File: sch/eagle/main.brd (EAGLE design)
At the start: 49.2 x 41.9 mm, 19 parts, among them IC1 LM339N

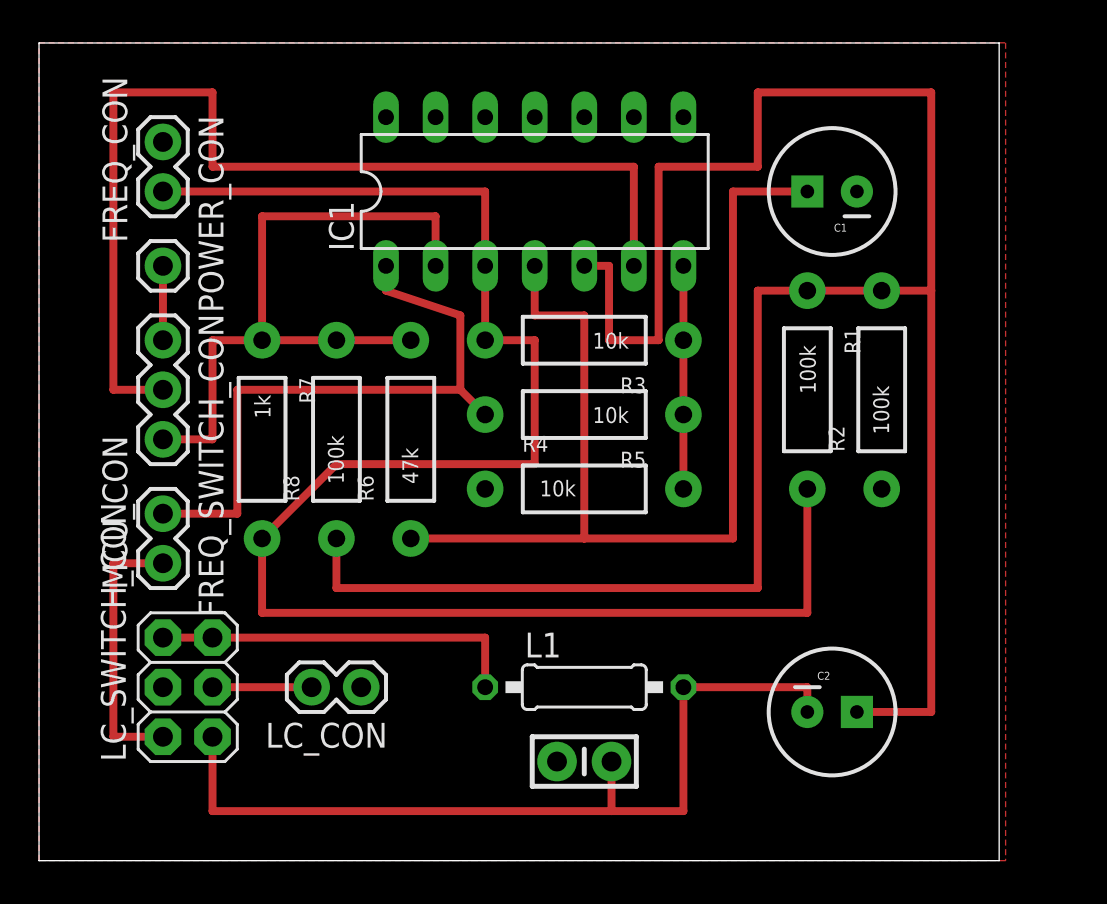
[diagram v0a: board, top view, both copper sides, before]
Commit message: [ add ] eagle, board routing refined, wider tracks.
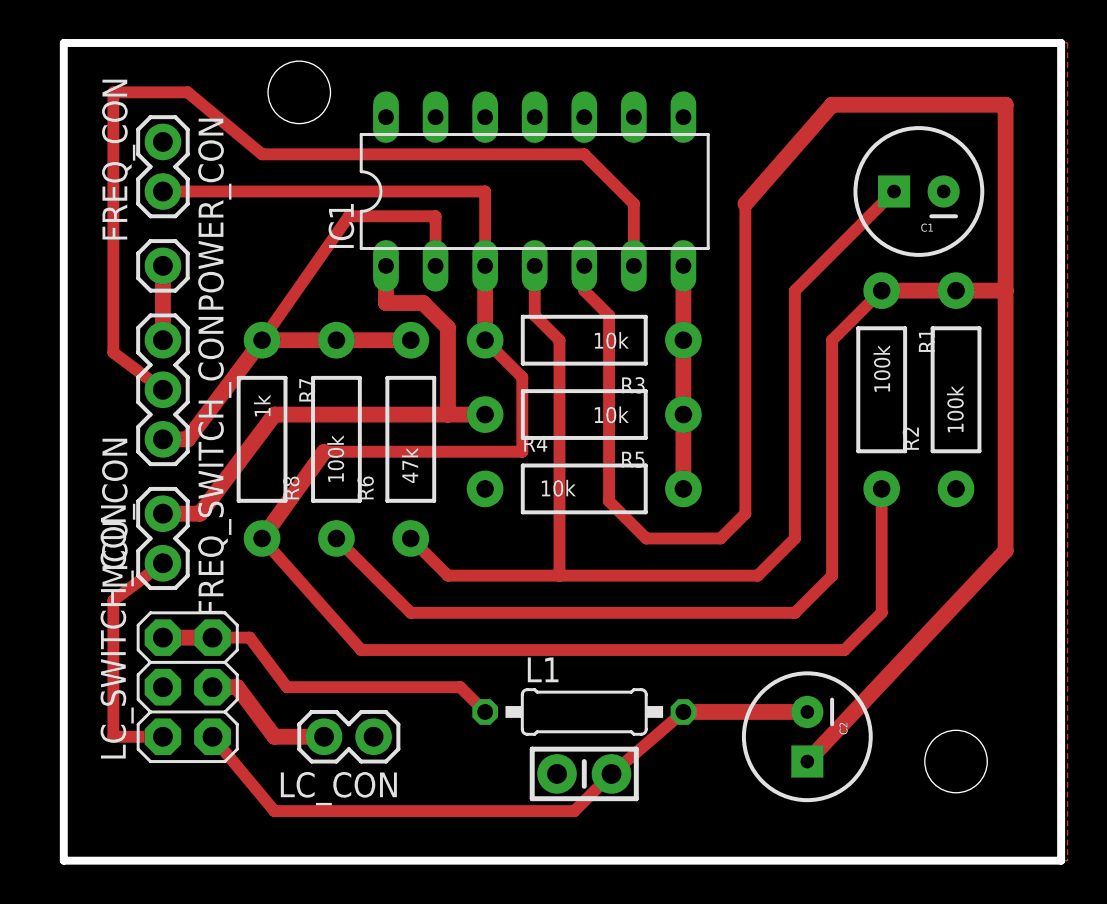
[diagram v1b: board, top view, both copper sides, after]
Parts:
- moved C1 4.45 mm to (42.5, 31.8)
- moved R1 3.81 mm to (40.6, 21.6)
- moved R2 3.81 mm to (44.5, 21.6)
- moved LC_CON 2.62 mm to (14.6, 3.81)
- moved C2 1.80 mm to (36.8, 3.81), turned to 270 degrees
- moved L1 1.27 mm to (25.4, 5.08)
- moved C3 0.64 mm to (25.4, 1.91)
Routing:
- net N$2: track 118.1 -> 139.9 mm
- net LC_SWITCH_C: track 44.5 -> 34.2 mm
- net LM_OUT: track 35.6 -> 30.0 mm
- net LM_IN: track 53.3 -> 48.6 mm
- net MCU_FREQ_CNT: track 32.5 -> 29.1 mm
- net N$5: track 54.6 -> 57.5 mm
- net LC_CON_PLUS: track 5.08 -> 6.99 mm
- net MCU_LC_SENSE: track 14.0 -> 12.7 mm
- net VREG_5V: track 86.7 -> 87.7 mm
- net LC_SWITCH_L: track 19.1 -> 18.3 mm
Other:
- board size 49.2 x 41.9 mm -> 51.1 x 41.9 mm

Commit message: [ update ] eagle, larger vias
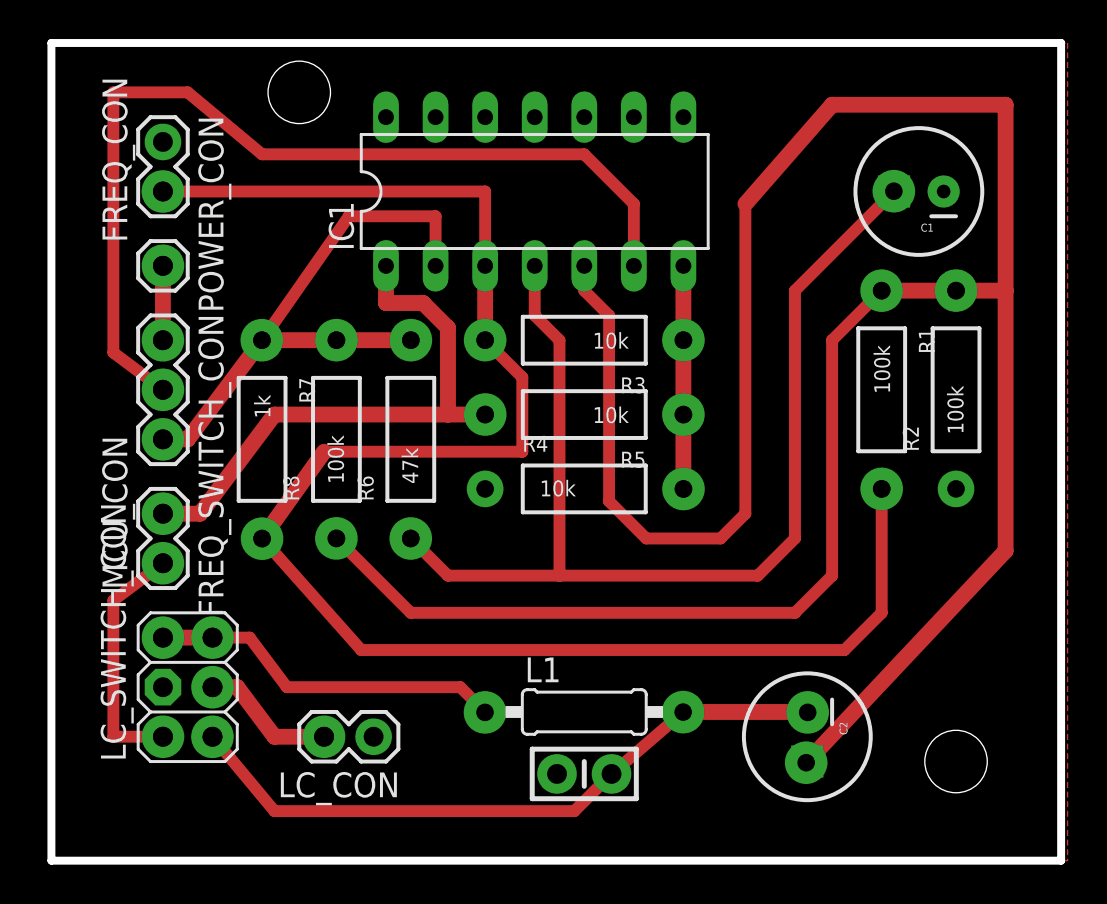
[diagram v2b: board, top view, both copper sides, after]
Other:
- board size 51.1 x 41.9 mm -> 51.7 x 41.9 mm
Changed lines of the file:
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@@
 <setting verticaltext="up"/>
 </settings>
-<grid distance="0.635" unitdist="mm" unit="mm" style="lines" multiple="1" display="yes" altdistance="0.025" altunitdist="inch" altunit="inch"/>
+<grid distance="0.025" unitdist="inch" unit="inch" style="lines" multiple="1" display="yes" altdistance="0.025" altunitdist="inch" altunit="inch"/>
 <layers>
 <layer number="1" name="Top" color="4" fill="1" visible="yes" active="yes"/>
@@
 <board>
 <plain>
-<wire x1="-1.27" y1="-2.54" x2="49.835" y2="-2.54" width="0.4064" layer="20"/>
+<wire x1="-1.905" y1="-2.54" x2="49.835" y2="-2.54" width="0.4064" layer="20"/>
 <wire x1="49.835" y1="-2.54" x2="49.835" y2="39.36" width="0.4064" layer="20"/>
-<wire x1="49.835" y1="39.36" x2="-1.27" y2="39.36" width="0.4064" layer="20"/>
-<wire x1="-1.27" y1="39.36" x2="-1.27" y2="-2.54" width="0.4064" layer="20"/>
+<wire x1="49.835" y1="39.36" x2="-1.905" y2="39.36" width="0.4064" layer="20"/>
+<wire x1="-1.905" y1="39.36" x2="-1.905" y2="-2.54" width="0.4064" layer="20"/>
 <hole x="44.45" y="2.54" drill="3.2"/>
 <hole x="10.795" y="36.83" drill="3.2"/>
@@
 <contactref element="LC_CON" pad="1"/>
 <polygon width="0.6096" layer="1" isolate="0.3048">
-<vertex x="-1.27" y="39.37"/>
+<vertex x="-1.905" y="39.37"/>
 <vertex x="50.165" y="39.37"/>
 <vertex x="50.165" y="-2.54"/>
-<vertex x="-1.27" y="-2.54"/>
+<vertex x="-1.905" y="-2.54"/>
 </polygon>
 </signal>
@@
 <wire x1="18.415" y1="24.765" x2="18.415" y2="20.32" width="0.8128" layer="1"/>
 </signal>
+<signal name="N$3">
+<via x="3.806196875" y="31.750796875" extent="1-16" drill="1.015" diameter="2.1844"/>
+</signal>
+<signal name="N$4">
+<via x="3.809715625" y="27.943034375" extent="1-16" drill="1.015" diameter="2.1844"/>
+</signal>
+<signal name="N$7">
+<via x="3.80825" y="24.12735625" extent="1-16" drill="1.015" diameter="2.1844"/>
+</signal>
+<signal name="N$8">
+<via x="3.810190625" y="21.58698125" extent="1-16" drill="1.015" diameter="2.1844"/>
+</signal>
+<signal name="N$9">
+<via x="3.80896875" y="19.05006875" extent="1-16" drill="1.015" diameter="2.1844"/>
+</signal>
+<signal name="N$10">
+<via x="3.811475" y="15.23925625" extent="1-16" drill="1.015" diameter="2.1844"/>
+</signal>
+<signal name="N$11">
+<via x="3.810190625" y="12.701675" extent="1-16" drill="1.015" diameter="2.1844"/>
+</signal>
+<signal name="N$12">
+<via x="3.811090625" y="8.887134375" extent="1-16" drill="1.015" diameter="2.1844"/>
+</signal>
+<signal name="N$13">
+<via x="6.350728125" y="8.89019375" extent="1-16" drill="1.015" diameter="2.1844"/>
+</signal>
+<signal name="N$15">
+<via x="6.349525" y="6.348225" extent="1-16" drill="1.015" diameter="2.1844"/>
+</signal>
+<signal name="N$16">
+<via x="3.811475" y="3.811575" extent="1-16" drill="1.015" diameter="2.1844"/>
+</signal>
+<signal name="N$17">
+<via x="6.34659375" y="3.808346875" extent="1-16" drill="1.015" diameter="2.1844"/>
+</signal>
+<signal name="N$18">
+<via x="12.06615" y="3.8098125" extent="1-16" drill="1.015" diameter="2.1844"/>
+</signal>
+<signal name="N$20">
+<via x="41.263428125" y="31.765615625" extent="1-16" drill="0.9" diameter="2.1844"/>
+</signal>
+<signal name="N$22">
+<via x="44.451921875" y="26.67256875" extent="1-16" drill="0.9" diameter="2.1844"/>
+</signal>
+<signal name="N$23">
+<via x="40.6369625" y="26.668696875" extent="1-16" drill="0.9" diameter="2.1844"/>
+</signal>
+<signal name="N$24">
+<via x="8.876046875" y="24.129825" extent="1-16" drill="0.9" diameter="2.1844"/>
+</signal>
+<signal name="N$25">
+<via x="12.701396875" y="24.132928125" extent="1-16" drill="0.9" diameter="2.1844"/>
+</signal>
+<signal name="N$26">
+<via x="16.51388125" y="24.132359375" extent="1-16" drill="0.9" diameter="2.1844"/>
+</signal>
+<signal name="N$27">
+<via x="20.319903125" y="24.13489375" extent="1-16" drill="0.9" diameter="2.1844"/>
+</signal>
+<signal name="N$28">
+<via x="30.481240625" y="24.1346875" extent="1-16" drill="0.9" diameter="2.1844"/>
+</signal>
+<signal name="N$29">
+<via x="20.325040625" y="20.321778125" extent="1-16" drill="0.9" diameter="2.1844"/>
+</signal>
+<signal name="N$30">
+<via x="30.480809375" y="20.316490625" extent="1-16" drill="0.9" diameter="2.1844"/>
+</signal>
+<signal name="N$31">
+<via x="30.483953125" y="16.504984375" extent="1-16" drill="0.9" diameter="2.1844"/>
+</signal>
+<signal name="N$33">
+<via x="8.888940625" y="13.96081875" extent="1-16" drill="0.9" diameter="2.1844"/>
+</signal>
+<signal name="N$34">
+<via x="12.69723125" y="13.975065625" extent="1-16" drill="0.9" diameter="2.1844"/>
+</signal>
+<signal name="N$35">
+<via x="16.50759375" y="13.970490625" extent="1-16" drill="0.9" diameter="2.1844"/>
+</signal>
+<signal name="N$36">
+<via x="20.313203125" y="5.05795" extent="1-16" drill="0.9" diameter="2.1844"/>
+</signal>
+<signal name="N$37">
+<via x="30.466596875" y="5.07224375" extent="1-16" drill="0.9" diameter="2.1844"/>
+</signal>
+<signal name="N$38">
+<via x="36.847853125" y="5.057684375" extent="1-16" drill="0.9" diameter="2.1844"/>
+</signal>
+<signal name="N$39">
+<via x="36.770434375" y="2.480896875" extent="1-16" drill="0.9" diameter="2.1844"/>
+</signal>
+<signal name="N$40">
+<via x="40.639575" y="16.511775" extent="1-16" drill="0.9" diameter="2.1844"/>
+</signal>
 </signals>
